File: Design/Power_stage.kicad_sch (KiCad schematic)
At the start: 39 parts, among them IC4 LM60440ARPKR, J15 Input Power, U3 CRE1S0505S3C, U6 CRE1S0505S3C, U8 LP3963-3.3

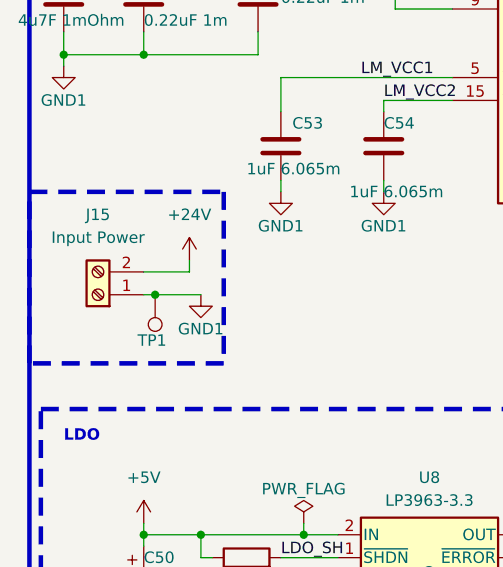
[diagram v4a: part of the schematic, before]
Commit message: PCB design started, comps arranged
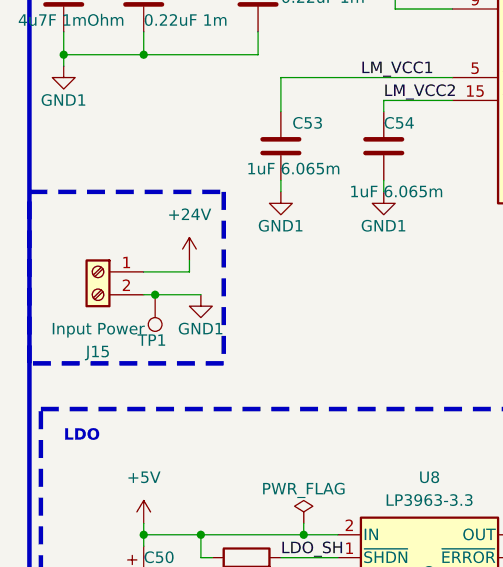
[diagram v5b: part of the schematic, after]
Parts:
- TP1, TP10, TP11, TP12, TP13, TP14, TP2, TP3, TP4, TP5, TP6, TP7, TP8, TP9: footprint TestPoint:TestPoint_Pad_D2.5mm -> TestPoint:TestPoint_Pad_D1.0mm
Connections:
- net +24V: now also J15.1 (Pin_1); no longer J15.2 (Pin_2)
- net GND1: now also J15.2 (Pin_2); no longer J15.1 (Pin_1)
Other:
- moved on the sheet: J15
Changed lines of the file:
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@@
   (junction (at 171.45 91.44) (diameter 0) (color 0 0 0 0)
   )
+  (junction (at 111.76 64.77) (diameter 0) (color 0 0 0 0)
+  )
   (junction (at 232.41 29.21) (diameter 0) (color 0 0 0 0)
   )
@@
   (junction (at 247.65 153.67) (diameter 0) (color 0 0 0 0)
   )
-  (junction (at 111.76 64.77) (diameter 0) (color 0 0 0 0)
-  )
   (junction (at 138.43 26.67) (diameter 0) (color 0 0 0 0)
   )
@@
     (stroke (width 0) (type default))
   )
+  (wire (pts (xy 110.49 64.77) (xy 111.76 64.77))
+    (stroke (width 0) (type default))
+  )
   (wire (pts (xy 137.16 53.34) (xy 137.16 52.07))
     (stroke (width 0) (type default))
@@
   )
   (wire (pts (xy 123.19 26.67) (xy 138.43 26.67))
-    (stroke (width 0) (type default))
-  )
-  (wire (pts (xy 111.76 64.77) (xy 110.49 64.77))
     (stroke (width 0) (type default))
   )
@@
       (effects (font (size 1.27 1.27)) (justify left) hide)
     )
-    (property "Footprint" "TestPoint:TestPoint_Pad_D2.5mm" (at 182.88 88.9 0)
+    (property "Footprint" "TestPoint:TestPoint_Pad_D1.0mm" (at 182.88 88.9 0)
       (effects (font (size 1.27 1.27)) hide)
     )
@@
       (effects (font (size 1.27 1.27)) (justify left) hide)
     )
-    (property "Footprint" "TestPoint:TestPoint_Pad_D2.5mm" (at 280.67 115.57 0)
+    (property "Footprint" "TestPoint:TestPoint_Pad_D1.0mm" (at 280.67 115.57 0)
       (effects (font (size 1.27 1.27)) hide)
     )
@@
       (effects (font (size 1.27 1.27)) (justify left) hide)
     )
-    (property "Footprint" "TestPoint:TestPoint_Pad_D2.5mm" (at 252.73 115.57 0)
+    (property "Footprint" "TestPoint:TestPoint_Pad_D1.0mm" (at 252.73 115.57 0)
       (effects (font (size 1.27 1.27)) hide)
     )
@@
       (effects (font (size 1.27 1.27)) (justify left) hide)
     )
-    (property "Footprint" "TestPoint:TestPoint_Pad_D2.5mm" (at 207.01 63.5 0)
+    (property "Footprint" "TestPoint:TestPoint_Pad_D1.0mm" (at 207.01 63.5 0)
       (effects (font (size 1.27 1.27)) hide)
     )
@@
       (effects (font (size 1.27 1.27)) (justify left) hide)
     )
-    (property "Footprint" "TestPoint:TestPoint_Pad_D2.5mm" (at 128.27 26.67 0)
+    (property "Footprint" "TestPoint:TestPoint_Pad_D1.0mm" (at 128.27 26.67 0)
       (effects (font (size 1.27 1.27)) hide)
     )
@@
       (effects (font (size 1.27 1.27)) (justify left) hide)
     )
-    (property "Footprint" "TestPoint:TestPoint_Pad_D2.5mm" (at 280.67 143.51 0)
+    (property "Footprint" "TestPoint:TestPoint_Pad_D1.0mm" (at 280.67 143.51 0)
       (effects (font (size 1.27 1.27)) hide)
     )
@@
       (effects (font (size 1.27 1.27)) (justify left) hide)
     )
-    (property "Footprint" "TestPoint:TestPoint_Pad_D2.5mm" (at 252.73 153.67 0)
+    (property "Footprint" "TestPoint:TestPoint_Pad_D1.0mm" (at 252.73 153.67 0)
       (effects (font (size 1.27 1.27)) hide)
     )
@@
       (effects (font (size 1.27 1.27)) (justify left) hide)
     )
-    (property "Footprint" "TestPoint:TestPoint_Pad_D2.5mm" (at 281.94 153.67 0)
+    (property "Footprint" "TestPoint:TestPoint_Pad_D1.0mm" (at 281.94 153.67 0)
       (effects (font (size 1.27 1.27)) hide)
     )
@@
       (effects (font (size 1.27 1.27)) (justify left) hide)
     )
-    (property "Footprint" "TestPoint:TestPoint_Pad_D2.5mm" (at 106.68 64.77 0)
+    (property "Footprint" "TestPoint:TestPoint_Pad_D1.0mm" (at 106.68 64.77 0)
       (effects (font (size 1.27 1.27)) hide)
     )
@@
       (effects (font (size 1.27 1.27)) (justify left) hide)
     )
-    (property "Footprint" "TestPoint:TestPoint_Pad_D2.5mm" (at 237.49 29.21 0)
+    (property "Footprint" "TestPoint:TestPoint_Pad_D1.0mm" (at 237.49 29.21 0)
       (effects (font (size 1.27 1.27)) hide)
     )
@@
       (effects (font (size 1.27 1.27)) (justify left) hide)
     )
-    (property "Footprint" "TestPoint:TestPoint_Pad_D2.5mm" (at 252.73 143.51 0)
+    (property "Footprint" "TestPoint:TestPoint_Pad_D1.0mm" (at 252.73 143.51 0)
       (effects (font (size 1.27 1.27)) hide)
     )
@@
       (effects (font (size 1.27 1.27)) (justify left) hide)
     )
-    (property "Footprint" "TestPoint:TestPoint_Pad_D2.5mm" (at 252.73 125.73 0)
+    (property "Footprint" "TestPoint:TestPoint_Pad_D1.0mm" (at 252.73 125.73 0)
       (effects (font (size 1.27 1.27)) hide)
     )
@@
       (effects (font (size 1.27 1.27)) (justify left) hide)
     )
-    (property "Footprint" "TestPoint:TestPoint_Pad_D2.5mm" (at 280.67 125.73 0)
+    (property "Footprint" "TestPoint:TestPoint_Pad_D1.0mm" (at 280.67 125.73 0)
       (effects (font (size 1.27 1.27)) hide)
     )
@@
     )
   )
-  (symbol (lib_id "Connector:Screw_Terminal_01x02") (at 105.41 64.77 180) (unit 1)
-    (in_bom yes) (on_board yes) (dnp no) (fields_autoplaced)
-    (property "Reference" "J15" (at 105.41 55.88 0)
-      (effects (font (size 1.27 1.27)))
-    )
-    (property "Value" "Input Power" (at 105.41 58.42 0)
-      (effects (font (size 1.27 1.27)))
-    )
-    (property "Footprint" "TerminalBlock_Phoenix:TerminalBlock_Phoenix_MKDS-1,5-2_1x02_P5.00mm_Horizontal" (at 105.41 64.77 0)
-      (effects (font (size 1.27 1.27)) hide)
-    )
-    (property "Datasheet" "~" (at 105.41 64.77 0)
+  (symbol (lib_id "Connector:Screw_Terminal_01x02") (at 105.41 62.23 0) (mirror y) (unit 1)
+    (in_bom yes) (on_board yes) (dnp no)
+    (property "Reference" "J15" (at 105.41 71.12 0)
+      (effects (font (size 1.27 1.27)))
+    )
+    (property "Value" "Input Power" (at 105.41 68.58 0)
+      (effects (font (size 1.27 1.27)))
+    )
+    (property "Footprint" "TerminalBlock_Phoenix:TerminalBlock_Phoenix_MKDS-1,5-2_1x02_P5.00mm_Horizontal" (at 105.41 62.23 0)
+      (effects (font (size 1.27 1.27)) hide)
+    )
+    (property "Datasheet" "~" (at 105.41 62.23 0)
       (effects (font (size 1.27 1.27)) hide)
     )
@@
       (effects (font (size 1.27 1.27)) (justify left) hide)
     )
-    (property "Footprint" "TestPoint:TestPoint_Pad_D2.5mm" (at 200.66 63.5 0)
-      (effects (font (size 1.27 1.27)) hide)
-    )
+    (property "Footprint" "TestPoint:TestPoint_Pad_D1.0mm" (at 200.66 63.5 0)
+      (effects (font (size 1.27 1.27)) hide)
+    )

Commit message: Added all the sections
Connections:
- net LM_VCC2 is gone; now on net LM_VCC: C54.1, IC4.15 (VCC_2)
- net LM_SW_1 renamed LM_SW
- net LM_VCC1 renamed LM_VCC
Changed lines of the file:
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@@
     (fill (type none))
   )
-  (rectangle (start 97.79 53.34) (end 119.38 72.39)
+  (rectangle (start 99.06 53.34) (end 120.65 72.39)
     (stroke (width 0.5) (type dash))
     (fill (type none))
@@
     (effects (font (size 1.27 1.27)) (justify left bottom))
   )
-  (label "LM_SW_2" (at 182.88 31.75 0) (fields_autoplaced)
+  (label "LM_SW" (at 182.88 31.75 0) (fields_autoplaced)
     (effects (font (size 1.27 1.27)) (justify left bottom))
   )
-  (label "LM_VCC1" (at 134.62 40.64 0) (fields_autoplaced)
+  (label "LM_VCC" (at 134.62 40.64 0) (fields_autoplaced)
     (effects (font (size 1.27 1.27)) (justify left bottom))
   )
-  (label "LM_VCC2" (at 137.16 43.18 0) (fields_autoplaced)
+  (label "LM_VCC" (at 137.16 43.18 0) (fields_autoplaced)
     (effects (font (size 1.27 1.27)) (justify left bottom))
   )
-  (label "LM_SW_1" (at 182.88 29.21 0) (fields_autoplaced)
+  (label "LM_SW" (at 182.88 29.21 0) (fields_autoplaced)
     (effects (font (size 1.27 1.27)) (justify left bottom))
   )
@@
   (symbol (lib_id "Connector:Screw_Terminal_01x02") (at 105.41 62.23 0) (mirror y) (unit 1)
     (in_bom yes) (on_board yes) (dnp no)
-    (property "Reference" "J15" (at 105.41 71.12 0)
-      (effects (font (size 1.27 1.27)))
-    )
-    (property "Value" "Input Power" (at 105.41 68.58 0)
-      (effects (font (size 1.27 1.27)))
-    )
+    (property "Reference" "J15" (at 105.41 67.31 0)
+      (effects (font (size 1.27 1.27)))
+    )
+    (property "Value" "Input Power" (at 106.68 58.42 0)
+      (effects (font (size 1.27 1.27)))
+    )

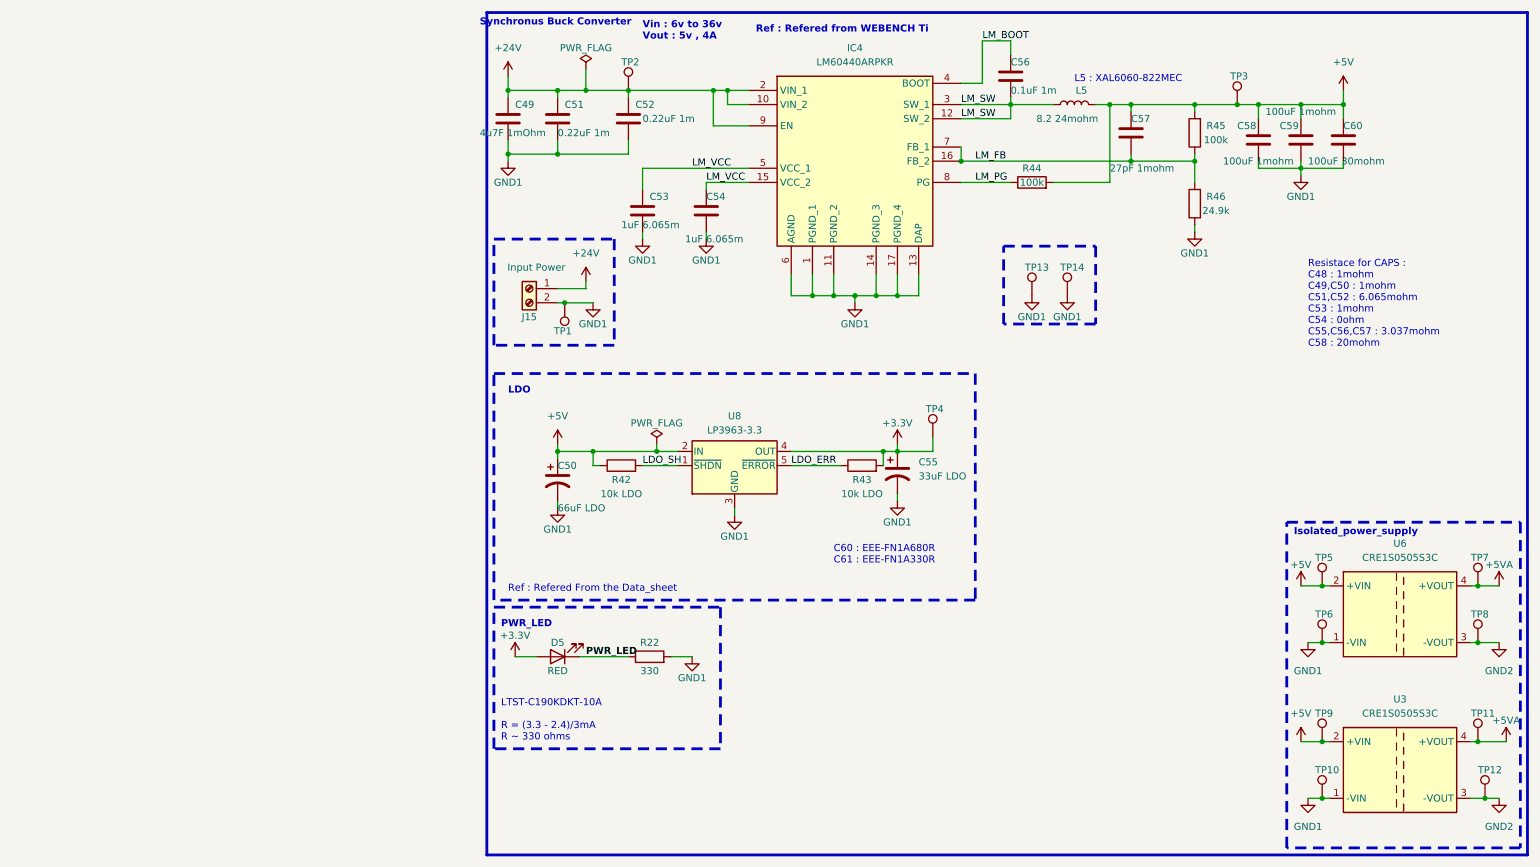
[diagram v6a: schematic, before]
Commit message: Added lib folder, Layer layed
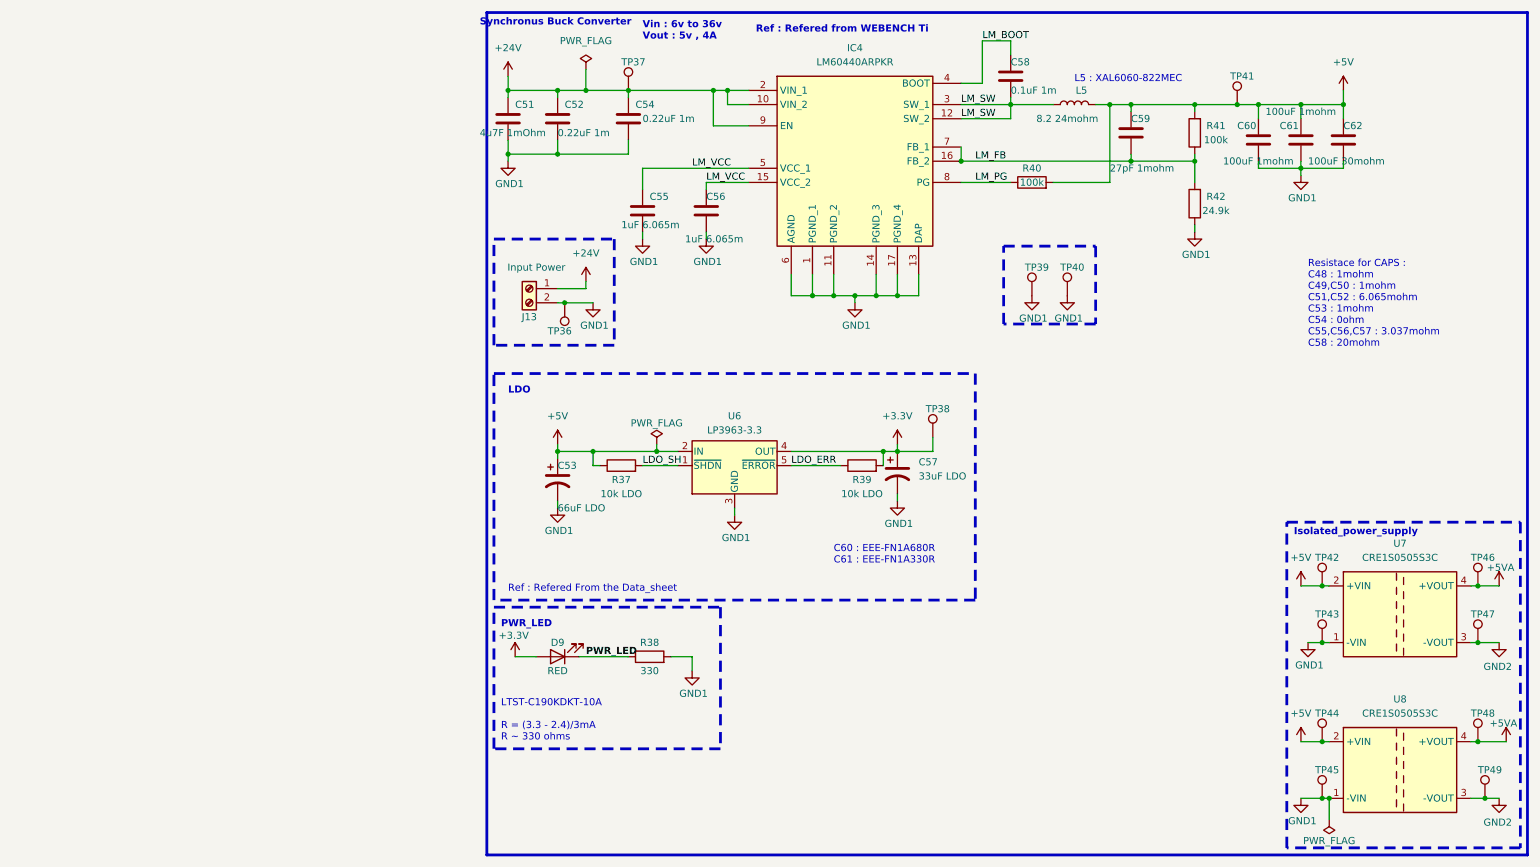
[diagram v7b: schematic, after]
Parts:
- renumbered C49 to C51, C51 to C52, C50 to C53, C52 to C54, C53 to C55, C54 to C56, C55 to C57, C56 to C58, C57 to C59, C58 to C60, C59 to C61, C60 to C62, D5 to D9, J15 to J13, R42 to R37, R22 to R38, R43 to R39, R44 to R40, R45 to R41, R46 to R42, TP1 to TP36, TP2 to TP37, TP4 to TP38, TP13 to TP39, TP14 to TP40, TP3 to TP41, TP5 to TP42, TP6 to TP43, TP9 to TP44, TP10 to TP45, TP7 to TP46, TP8 to TP47, TP11 to TP48, TP12 to TP49, U8 to U6, U6 to U7, U3 to U8

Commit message: End of version 1.0.0 design
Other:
- title: (none) -> Rapid-Core
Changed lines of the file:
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@@
 	(generator_version "8.0")
 	(paper "A4")
+	(title_block
+		(title "Rapid-Core")
+		(date "2024-09-09")
+		(rev "1.0.0")
+	)
 	(junction
 		(at 275.59 125.73)
@@
 	(text "Synchronus Buck Converter"
 		(exclude_from_sim no)
-		(at 96.52 15.24 0)
+		(at 98.298 15.24 0)
 		(effects
 			(font
